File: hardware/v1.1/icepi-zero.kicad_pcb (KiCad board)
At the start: 4 copper layers, 65 x 30 mm, 143 parts, among them J1 Conn_02x20_Counter_Clockwise, J2 HDMI_C_1.3, J3 USB_C_Receptacle_USB2.0_14P, J4 USB_C_Receptacle_USB2.0_14P, J5 USB_C_Receptacle_USB2.0_14P, J6 Micro_SD_Card_Det2, SW1 SW_Push, SW2 SW_Push, U1 ECP5U_12_CABGA256, U10 W9825G6KH, U11 W25Q128JVS, U2 TLV62569DBV, U3 TLV62569DBV, U4 TLV62569DBV, U5 PCA9306DC1, U6 FT231XQ, U7 TPD2EUSB30A, U8 TPD2EUSB30A, U9 TPD2EUSB30A, Y1 SITxxxxxx-1x-33E-50.000000

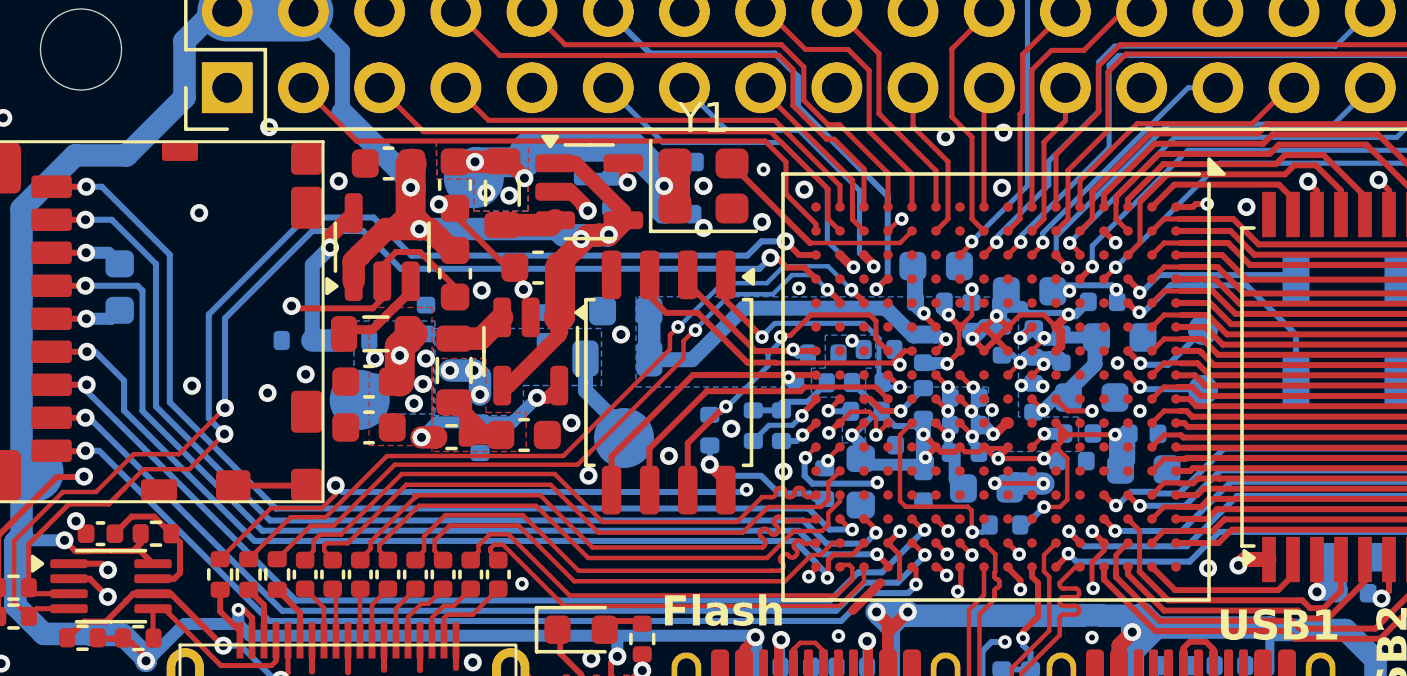
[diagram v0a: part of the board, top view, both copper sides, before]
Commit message: Clean up the design by a bit
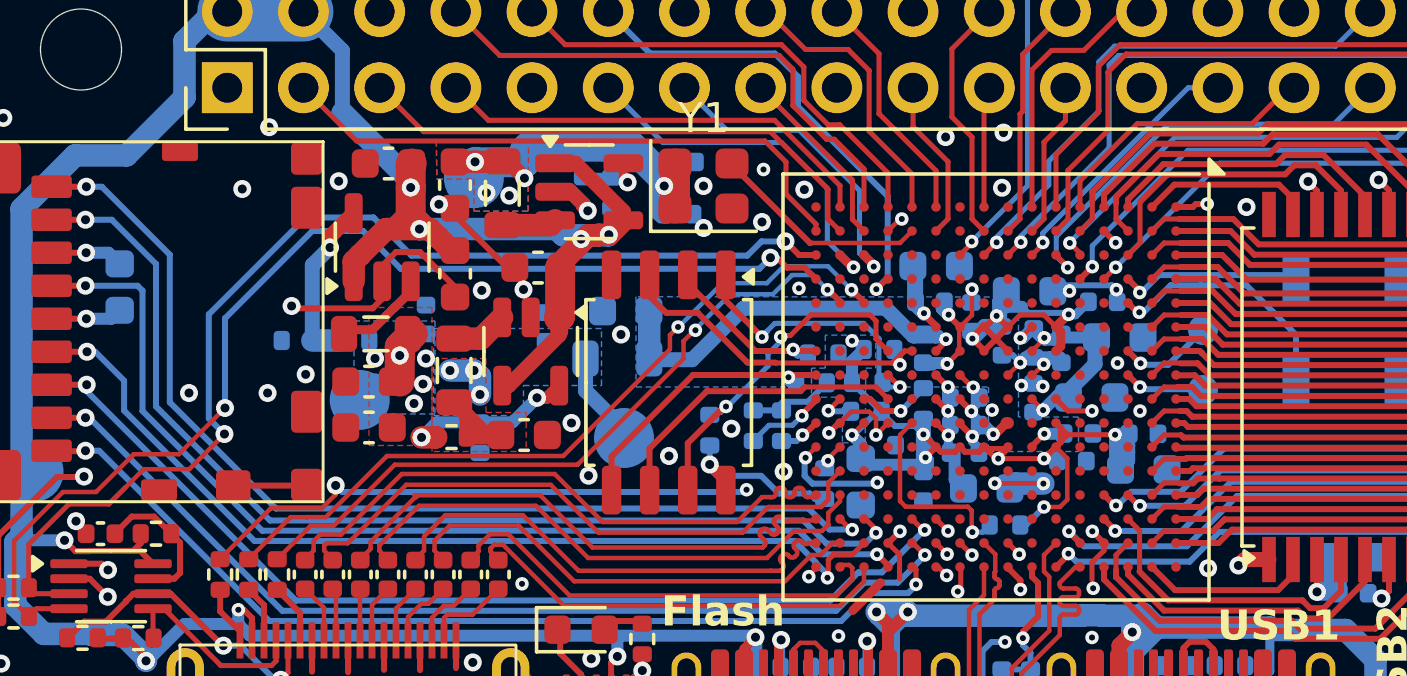
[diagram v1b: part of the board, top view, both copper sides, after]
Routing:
- net +3V3: track 99.9 -> 102.2 mm
- net GND: track 79.2 -> 80.3 mm

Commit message: Board type
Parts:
- U1: value ECP5U_12_CABGA256 -> ECP5U_25F_CABGA256
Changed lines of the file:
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@@
 			)
 		)
-		(property "Value" "ECP5U_12_CABGA256"
+		(property "Value" "ECP5U_25F_CABGA256"
 			(at 0 8.2 90)
 			(layer "F.Fab")

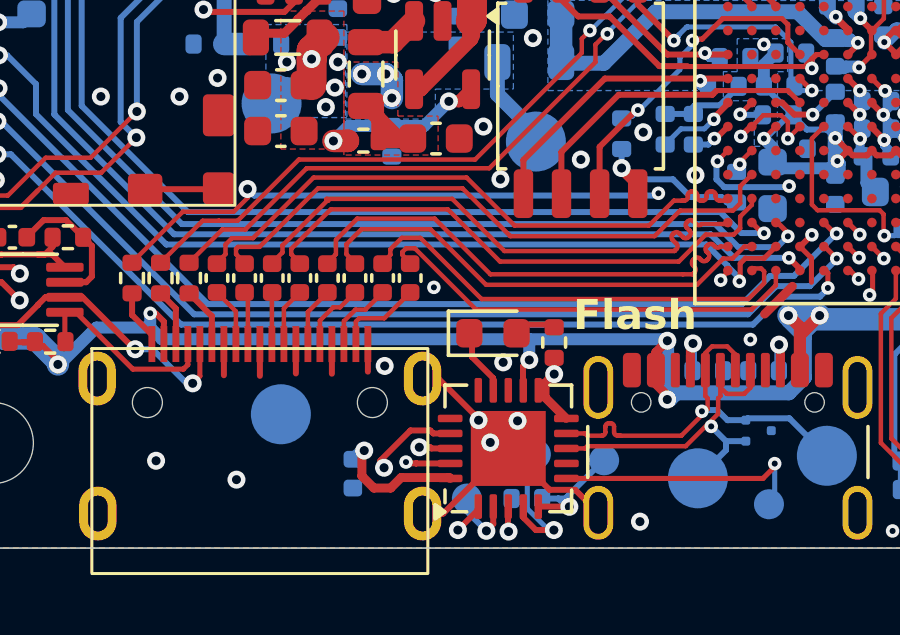
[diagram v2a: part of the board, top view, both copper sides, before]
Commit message: Correct solder keepout on mounting points and move resistors
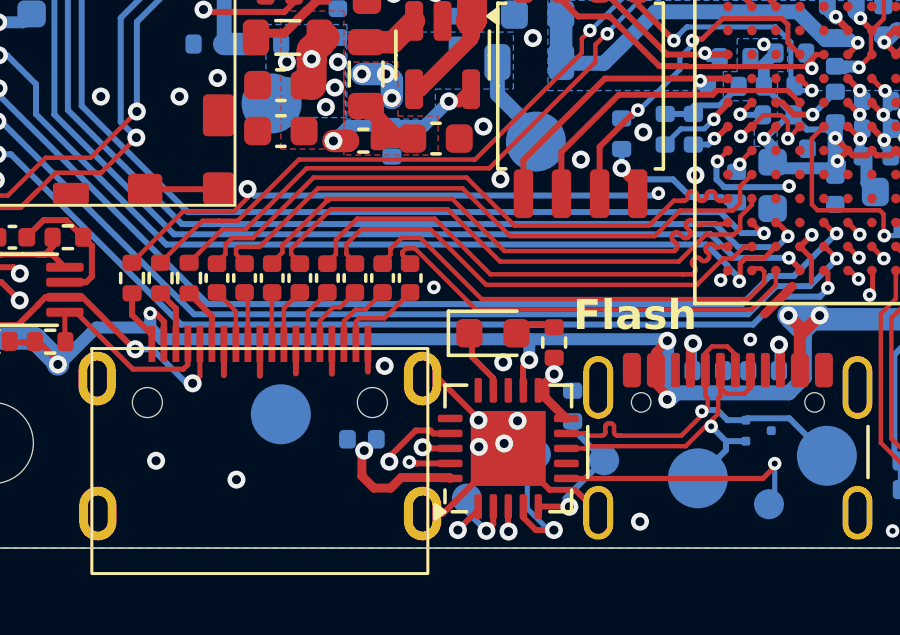
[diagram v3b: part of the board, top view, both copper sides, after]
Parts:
- moved R25 3.44 mm to (138.8, 115.3), turned to 90 degrees
- moved C38 1.18 mm to (131.8, 116.4), turned to 180 degrees
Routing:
- net JTAG_TMS: track 36.9 -> 37.5 mm
- net USB_TXD: track 24.0 -> 23.4 mm
- net GND: vias 103 -> 104

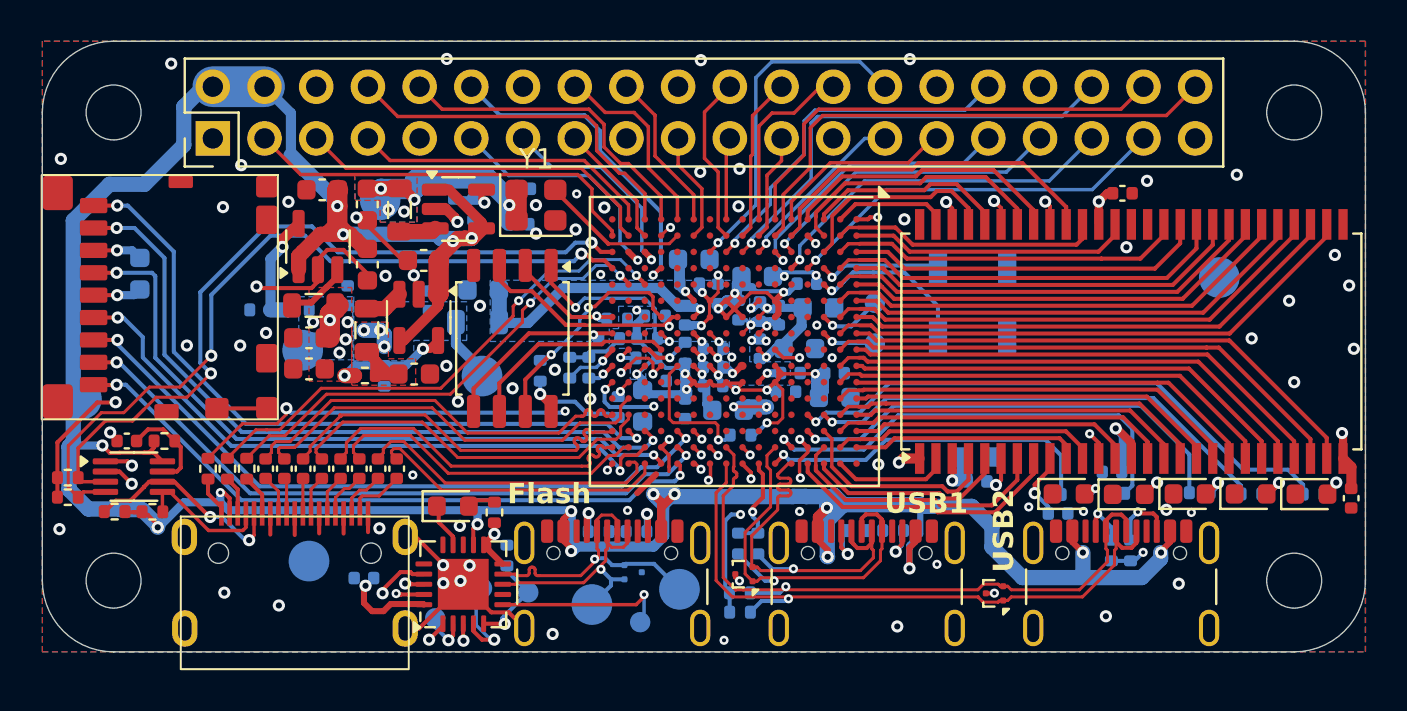
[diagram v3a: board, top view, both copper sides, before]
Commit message: Make routing more optimized
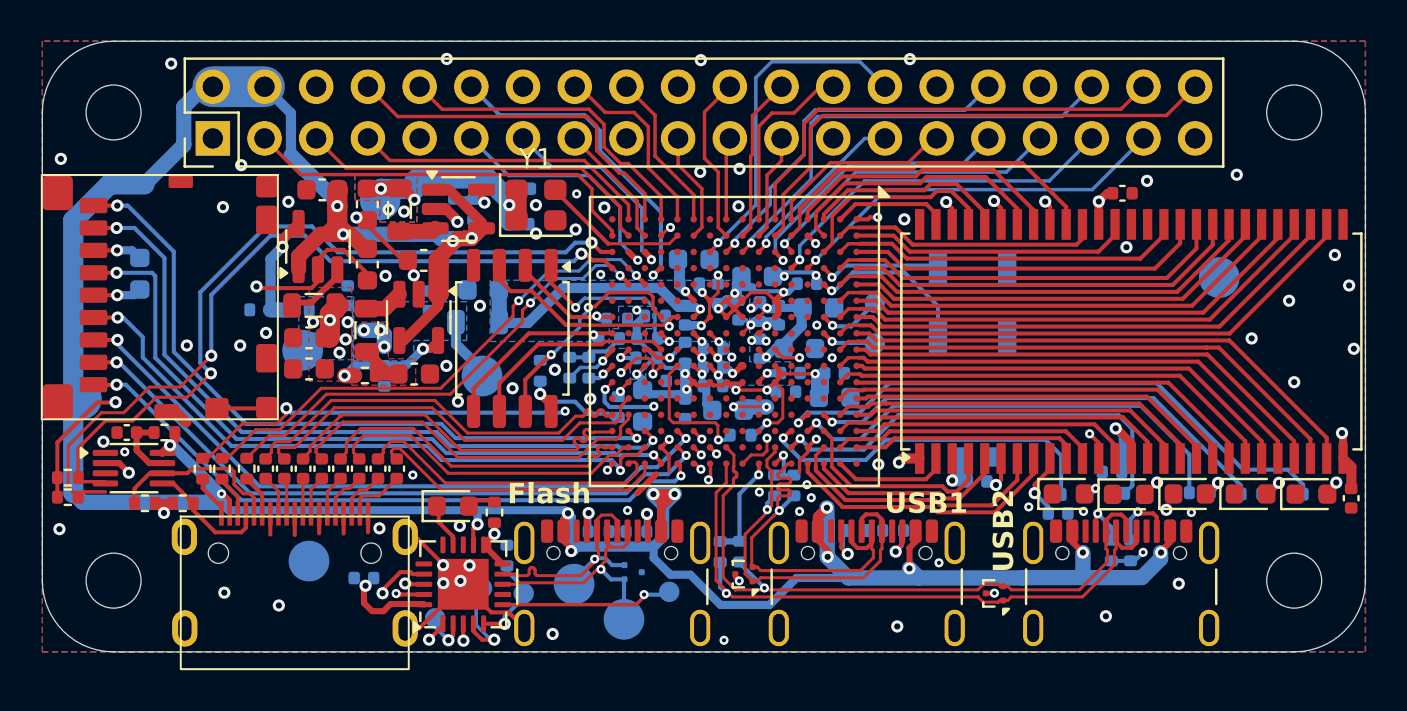
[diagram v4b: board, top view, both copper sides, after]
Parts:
- moved TP7 5.18 mm to (142.1, 116.7)
- moved R39 3.36 mm to (152.0, 111.8)
- moved R40 3.36 mm to (152.9, 111.8)
- moved R41 3.12 mm to (149.3, 115.1), turned to -90 degrees
- moved TP11 2.07 mm to (146.8, 117.0)
- moved R42 2.03 mm to (150.2, 115.1), turned to -90 degrees
- moved TP8 1.73 mm to (144.6, 118.4)
- moved R17 1.55 mm to (122.9, 112.7)
- moved R16 1.55 mm to (121.0, 112.7)
- moved C37 0.42 mm to (120.2, 109.2)
- moved R15 0.42 mm to (122.0, 109.2), turned to 180 degrees
- moved U5 0.42 mm to (120.5, 111.0)
- moved R13 0.27 mm to (124.8, 111.0)
- moved R14 0.27 mm to (123.9, 111.0)
- moved TP12 0.23 mm to (139.7, 117.1)
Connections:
- U1 pad E14: unconnected-(U1D-PR5C/+/RDQ8-PadE14) -> LED1
- U1 pad F16: LED1 -> USB2_PULL
- U1 pad G16: USB2_PULL -> USB3_PULL
- U1 pad H15: USB3_PULL -> unconnected-(U1D-PR20B/-/HS/RDQSN20-PadH15)
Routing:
- net +5V: track 223.8 -> 186.1 mm
- net USB3_PULL: track 9.55 -> 5.16 mm, vias 2 -> 1
- net +3V3: track 102.2 -> 99.1 mm
- net JTAG_TMS: track 37.5 -> 35.0 mm
- net JTAG_TCK: track 38.2 -> 35.9 mm
- net USB2_PULL: track 4.76 -> 2.51 mm
- net GND: track 80.3 -> 78.1 mm, vias 104 -> 106
- net GPDI_SCL: track 10.5 -> 8.73 mm, vias 2 -> 0
- net D1-: track 14.2 -> 12.6 mm
- net Net-(U5-VREF2): track 4.77 -> 3.26 mm
- net D2+: track 20.4 -> 19.1 mm
- net D2-: track 20.1 -> 19.1 mm
- net LED5: track 27.8 -> 28.8 mm
- net GPDI_SDA: track 7.01 -> 6.08 mm
- net FLASH_MOSI: track 9.68 -> 8.87 mm
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
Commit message: Improve HDMI spacing and impedance control
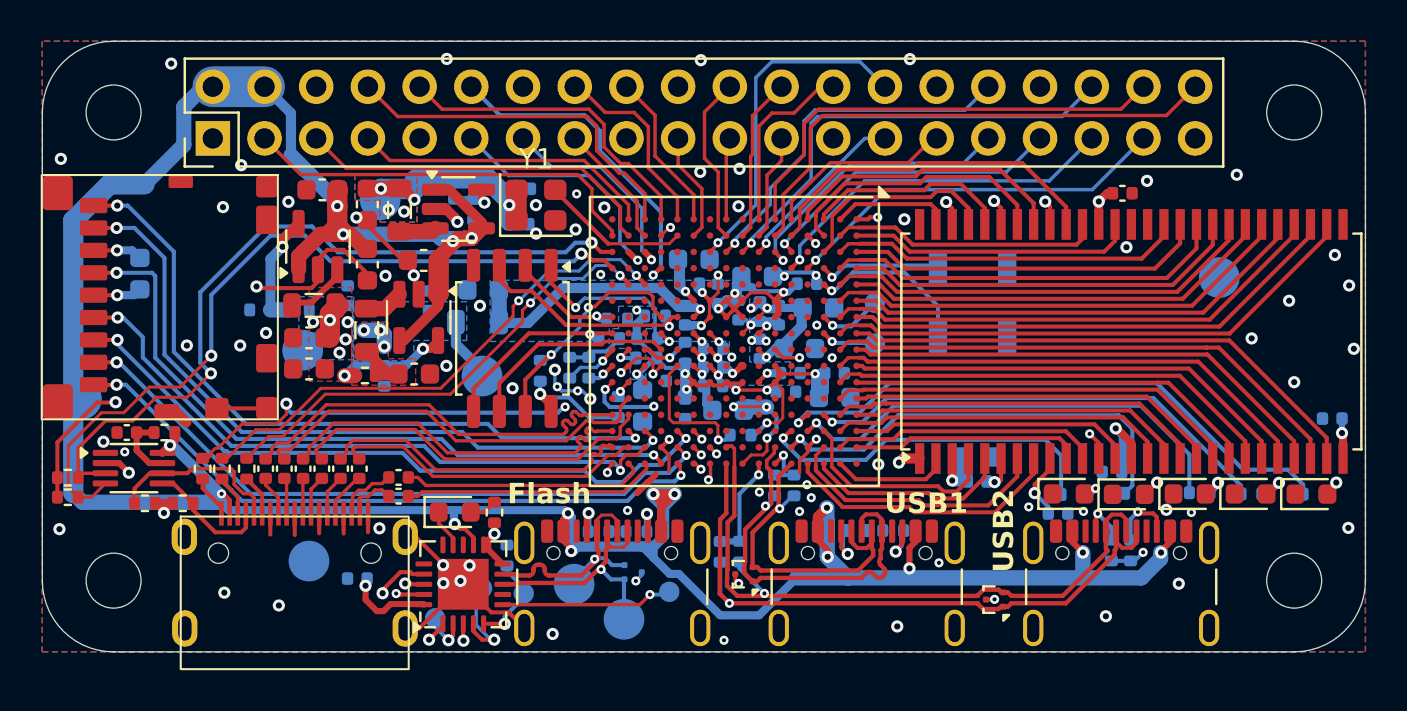
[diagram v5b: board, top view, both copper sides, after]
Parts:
- C39: moved to B.Cu
- moved C39 4.02 mm to (179.4, 108.5), turned to 180 degrees
- moved C29 1.35 mm to (133.5, 112.3), turned to 180 degrees
- moved C30 1.10 mm to (133.5, 111.4), turned to 180 degrees
- moved C38 0.33 mm to (131.5, 116.4)
- moved U8 0.31 mm to (162.8, 117.4)
- moved D6 0.30 mm to (136.3, 113.1)
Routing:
- net GND: track 78.1 -> 83.6 mm, vias 106 -> 107
- net FPDI_D2-: track 15.1 -> 12.0 mm
- net D2-: track 19.1 -> 16.6 mm
- net FPDI_D2+: track 14.6 -> 12.6 mm
- net +3V3: track 99.1 -> 97.7 mm
- net +5V: track 186.1 -> 187.1 mm
- net Net-(U6-3V3OUT): track 14.5 -> 13.8 mm
- net FPDI_HPD: track 26.7 -> 27.4 mm
- net D3+: track 32.4 -> 33.1 mm
- net ~{RXLED}: track 2.48 -> 1.90 mm
- net FPDI_D1-: track 16.1 -> 15.6 mm
- net /GPIO/CONN_D2-: track 2.45 -> 3.00 mm
- net D2+: track 19.1 -> 19.6 mm
- net JTAG_TDO: track 26.0 -> 25.5 mm

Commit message: OSHWA cerification :yay: and pinout diagram
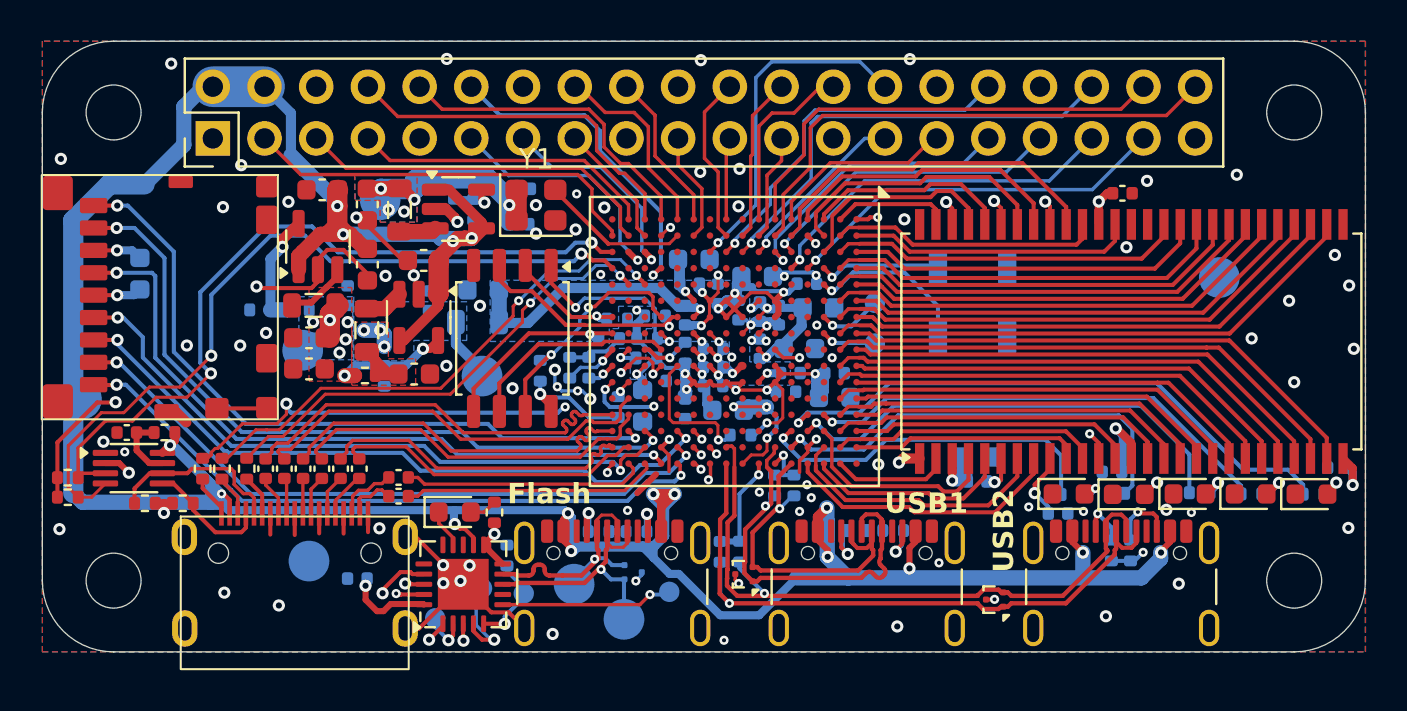
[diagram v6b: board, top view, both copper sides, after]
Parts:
- added LOGO1: ~, oshw:OSHW-Certification-Mark-Logo_6x3mm_SilkScreen, B.Cu at (177.7, 109.0)
- moved C39 2.42 mm to (179.6, 111.0)
- moved G*** 0.37 mm to (177.8, 98.8)
